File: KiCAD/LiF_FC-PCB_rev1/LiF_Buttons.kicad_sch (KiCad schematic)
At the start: 43 parts, among them J34 BTN 3V3_{EN}, J35 BTN 3V3_{EN}, SW10 TL3301PF160QG, SW11 TL3301PF160QG, SW4 TL3301PF160QG, SW5 TL3301PF160QG, SW6 TL3301PF160QG, SW7 TL3301PF160QG, SW8 TL3301PF160QG, SW9 TL3301PF160QG, U16 SN74HC14DR, U17 SN74HC14DR, U18 74HCT595PW,118

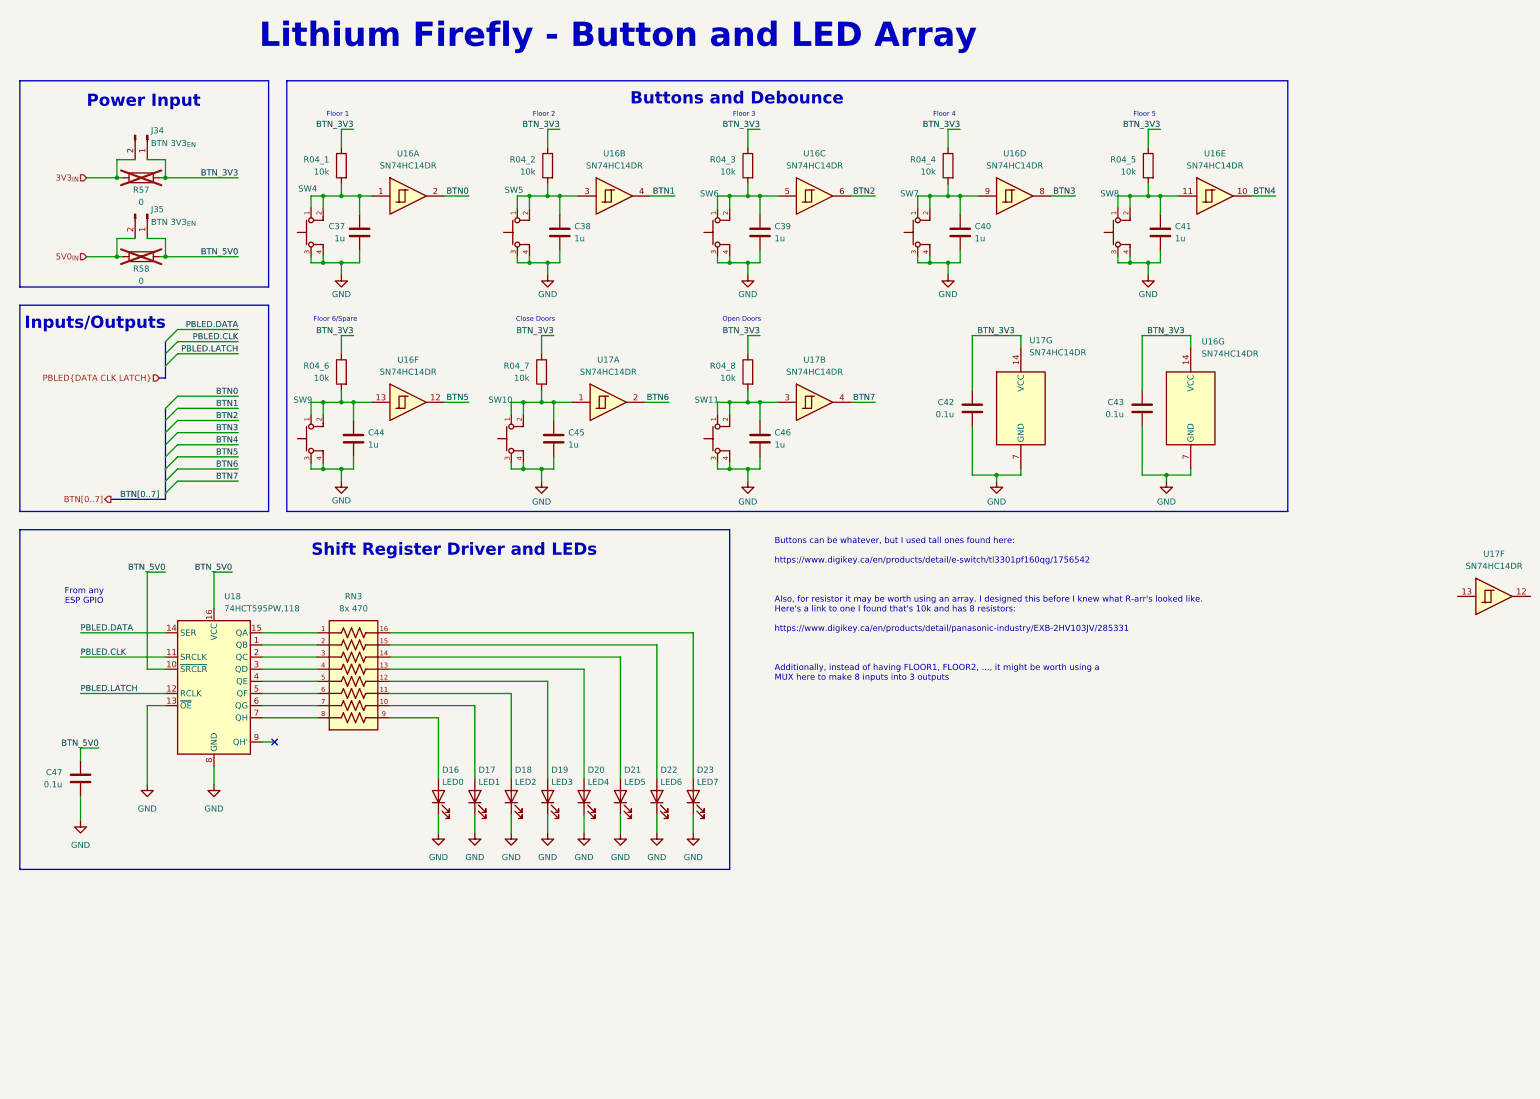
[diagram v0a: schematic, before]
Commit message: fixing ERC bugs on schematic. Only MCU left
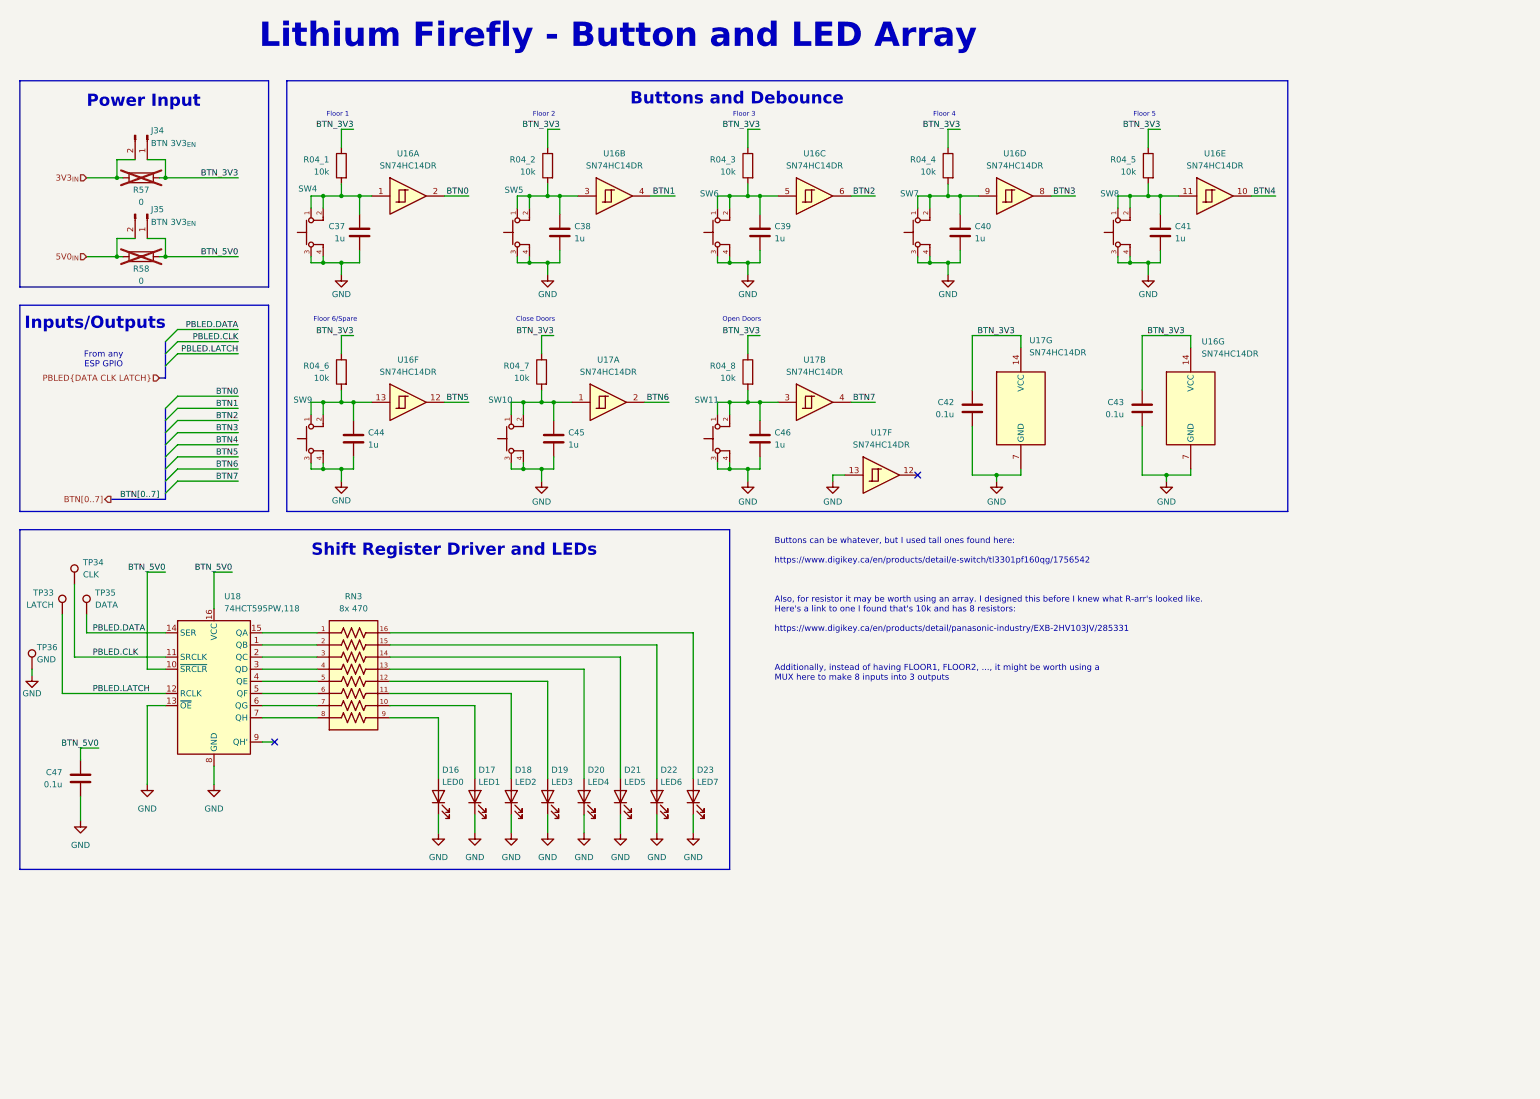
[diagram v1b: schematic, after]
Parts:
- added TP33: LATCH, TestPoint:TestPoint_Bridge_Pitch2.54mm_Drill1.0mm, symbol Connector:TestPoint
- added TP34: CLK, TestPoint:TestPoint_Bridge_Pitch2.54mm_Drill1.0mm, symbol Connector:TestPoint
- added TP35: DATA, TestPoint:TestPoint_Bridge_Pitch2.54mm_Drill1.0mm, symbol Connector:TestPoint
- added TP36: GND, TestPoint:TestPoint_Bridge_Pitch2.54mm_Drill1.0mm, symbol Connector:TestPoint
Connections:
- net GND: now also U17.13, TP36.1
- net PBLED.CLK: now also TP34.1
- net PBLED.DATA: now also TP35.1
- net PBLED.LATCH: now also TP33.1
- no-connect marks 1 -> 2
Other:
- moved on the sheet: U17F

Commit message: Added MCU pinout, shanged shift registers to GPIO expanders to save pins on MCU
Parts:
- removed C47: 0.1u, Capacitor_SMD:C_0805_2012Metric, symbol Device:C
- removed J35: BTN 3V3_{EN}, Connector_PinHeader_2.54mm:PinHeader_1x02_P2.54mm_Vertical, symbol Connector:Conn_01x02_Pin
- removed R58: 0, Resistor_SMD:R_0805_2012Metric, symbol Device:R
- removed TP33: LATCH, TestPoint:TestPoint_Bridge_Pitch2.54mm_Drill1.0mm, symbol Connector:TestPoint
- removed TP34: CLK, TestPoint:TestPoint_Bridge_Pitch2.54mm_Drill1.0mm, symbol Connector:TestPoint
- removed TP35: DATA, TestPoint:TestPoint_Bridge_Pitch2.54mm_Drill1.0mm, symbol Connector:TestPoint
- removed TP36: GND, TestPoint:TestPoint_Bridge_Pitch2.54mm_Drill1.0mm, symbol Connector:TestPoint
- removed U18: 74HCT595PW,118, Package_SO:TSSOP-16_4.4x5mm_P0.65mm, symbol 74xx:74HCT595
- added C45: 0.1u, Capacitor_SMD:C_0805_2012Metric, symbol Device:C
- added JP1: BTN3, Jumper:SolderJumper-2_P1.3mm_Open_RoundedPad1.0x1.5mm, symbol Jumper:SolderJumper_2_Open
- added JP2: BTN4, Jumper:SolderJumper-2_P1.3mm_Open_RoundedPad1.0x1.5mm, symbol Jumper:SolderJumper_2_Open
- added JP3: BTN5, Jumper:SolderJumper-2_P1.3mm_Open_RoundedPad1.0x1.5mm, symbol Jumper:SolderJumper_2_Open
- added R04_9: 10k, Resistor_SMD:R_0805_2012Metric, symbol Device:R
- added U18: NCA9555, Package_SO:TSSOP-24_4.4x7.8mm_P0.65mm, symbol Interface_Expansion:PCA9555PW
- renumbered C37 to C35, C38 to C36, C39 to C37, C40 to C38, C41 to C39, C42 to C40, C43 to C41, C44 to C42, C45 to C43, C46 to C44, U16 to U15, U17 to U16
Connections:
- net BTN0: now also U18.4 (IO0_0)
- net BTN1: now also U18.5 (IO0_1)
- net BTN2: now also U18.6 (IO0_2)
- net BTN3: now also JP1.2 (B), U18.7 (IO0_3); no longer U15.8
- net BTN4: now also JP2.1 (A), U18.8 (IO0_4); no longer U15.10
- net BTN5: now also JP3.2 (B), U18.9 (IO0_5); no longer U15.12
- net BTN6: now also U18.10 (IO0_6)
- net BTN7: now also U18.11 (IO0_7)
- net BTN_3V3: now also C45.1, R04_9.1, U18.24 (VDD)
- net GND: now also C45.2, U18.12 (VSS), U18.2 (A1), U18.21 (A0), U18.3 (A2)
- net LED1: now reaches RN3.2
- net LED1: now also U18.14 (IO1_1)
- net LED0: now reaches RN3.1
- net LED0: now also U18.13 (IO1_0)
- net LED2: now reaches RN3.3
- net LED2: now also U18.15 (IO1_2)
- net LED3: now reaches RN3.4
- net LED3: now also U18.16 (IO1_3)
- net LED4: now reaches RN3.5
- net LED4: now also U18.17 (IO1_4)
- net LED5: now reaches RN3.6
- net LED5: now also U18.18 (IO1_5)
- net LED6: now reaches RN3.7
- net LED6: now also U18.19 (IO1_6)
- net LED7: now reaches RN3.8
- net LED7: now also U18.20 (IO1_7)
- new net: JP1.1 (A), U15.8
- new net: JP2.2 (B), U15.10
- new net: JP3.1 (A), U15.12
- new net I2C.SCL: U18.22 (SCL)
- new net I2C.SDA: U18.23 (SDA)
- new net ~{BTN_IRQ}: R04_9.2, U18.1 (~{INT})
- no-connect marks 2 -> 1
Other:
- note added: "Floor Selection LEDs"
- note added: "I2C GPIO Expander"
- note added: "I2C addr 0100 000x"
- note removed: "From any ESP GPIO"
- note removed: "Shift Register Driver and LEDs"
- title: (none) -> Lithium Firefly Custom FC/CC PCB
- moved on the sheet: D16, D17, D18, D19, D20, D21, D22, D23, J34, R57, RN3

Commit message: Finalized schematic diagram. Only needs formatting fixes and resistor component sourcing info
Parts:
- renumbered C35 to C43, C36 to C44, C37 to C45, C38 to C46, C39 to C47, C40 to C48, C41 to C49, C42 to C50, C43 to C51, C44 to C52, C45 to C53, J34 to J38, R04_1 to R61, R04_2 to R62, R04_3 to R63, R04_4 to R64, R04_5 to R65, R57 to R66, R04_6 to R67, R04_7 to R68, R04_8 to R69, R04_9 to R70, U16 to U15, U15 to U16, U18 to U17

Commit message: added door limit switch and fixed I2C pull up resistors
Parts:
- added C57: 1u, Capacitor_SMD:C_0805_2012Metric, symbol Device:C
- added J43: Door Closed, symbol Connector_Generic:Conn_01x02
- added R76: 10k, Resistor_SMD:R_0805_2012Metric, symbol Device:R
- added R77: 100, Resistor_SMD:R_0805_2012Metric, symbol Device:R
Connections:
- net BTN_3V3: now also R76.1
- net GND: now also C57.2, J43.1 (Pin_1); no longer U16.13
- net DoorLS: now reaches U16.12
- new net: J43.2 (Pin_2), R76.2, R77.1
- new net: C57.1, R77.2, U16.13
- no-connect marks 1 -> 0
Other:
- note added: "Door Closed Switch"

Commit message: set up board configuration and started routing PCB
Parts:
- J43: footprint (none) -> Connector_JST:JST_PH_B2B-PH-K_1x02_P2.00mm_Vertical
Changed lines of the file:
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@@
 			)
 		)
-		(property "Footprint" ""
+		(property "Footprint" "Connector_JST:JST_PH_B2B-PH-K_1x02_P2.00mm_Vertical"
 			(at 198.12 148.59 0)
 			(effects

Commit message: backup before expanding the board size
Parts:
- removed JP1: BTN3, Jumper:SolderJumper-2_P1.3mm_Open_RoundedPad1.0x1.5mm, symbol Jumper:SolderJumper_2_Open
- removed JP2: BTN4, Jumper:SolderJumper-2_P1.3mm_Open_RoundedPad1.0x1.5mm, symbol Jumper:SolderJumper_2_Open
- removed JP3: BTN5, Jumper:SolderJumper-2_P1.3mm_Open_RoundedPad1.0x1.5mm, symbol Jumper:SolderJumper_2_Open
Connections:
- net BTN3: now also U15.8
- net BTN4: now also U15.10
- net BTN5: now also U15.12

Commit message: backup before leaving school
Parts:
- J38: footprint Connector_PinHeader_2.54mm:PinHeader_1x02_P2.54mm_Vertical -> Connector_PinHeader_2.54mm:PinHeader_1x02_P2.54mm_Vertical_SMD_Pin1Left
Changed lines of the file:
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@@
 			)
 		)
-		(property "Footprint" "Connector_PinHeader_2.54mm:PinHeader_1x02_P2.54mm_Vertical"
+		(property "Footprint" "Connector_PinHeader_2.54mm:PinHeader_1x02_P2.54mm_Vertical_SMD_Pin1Left"
 			(at 41.91 46.99 0)
 			(effects

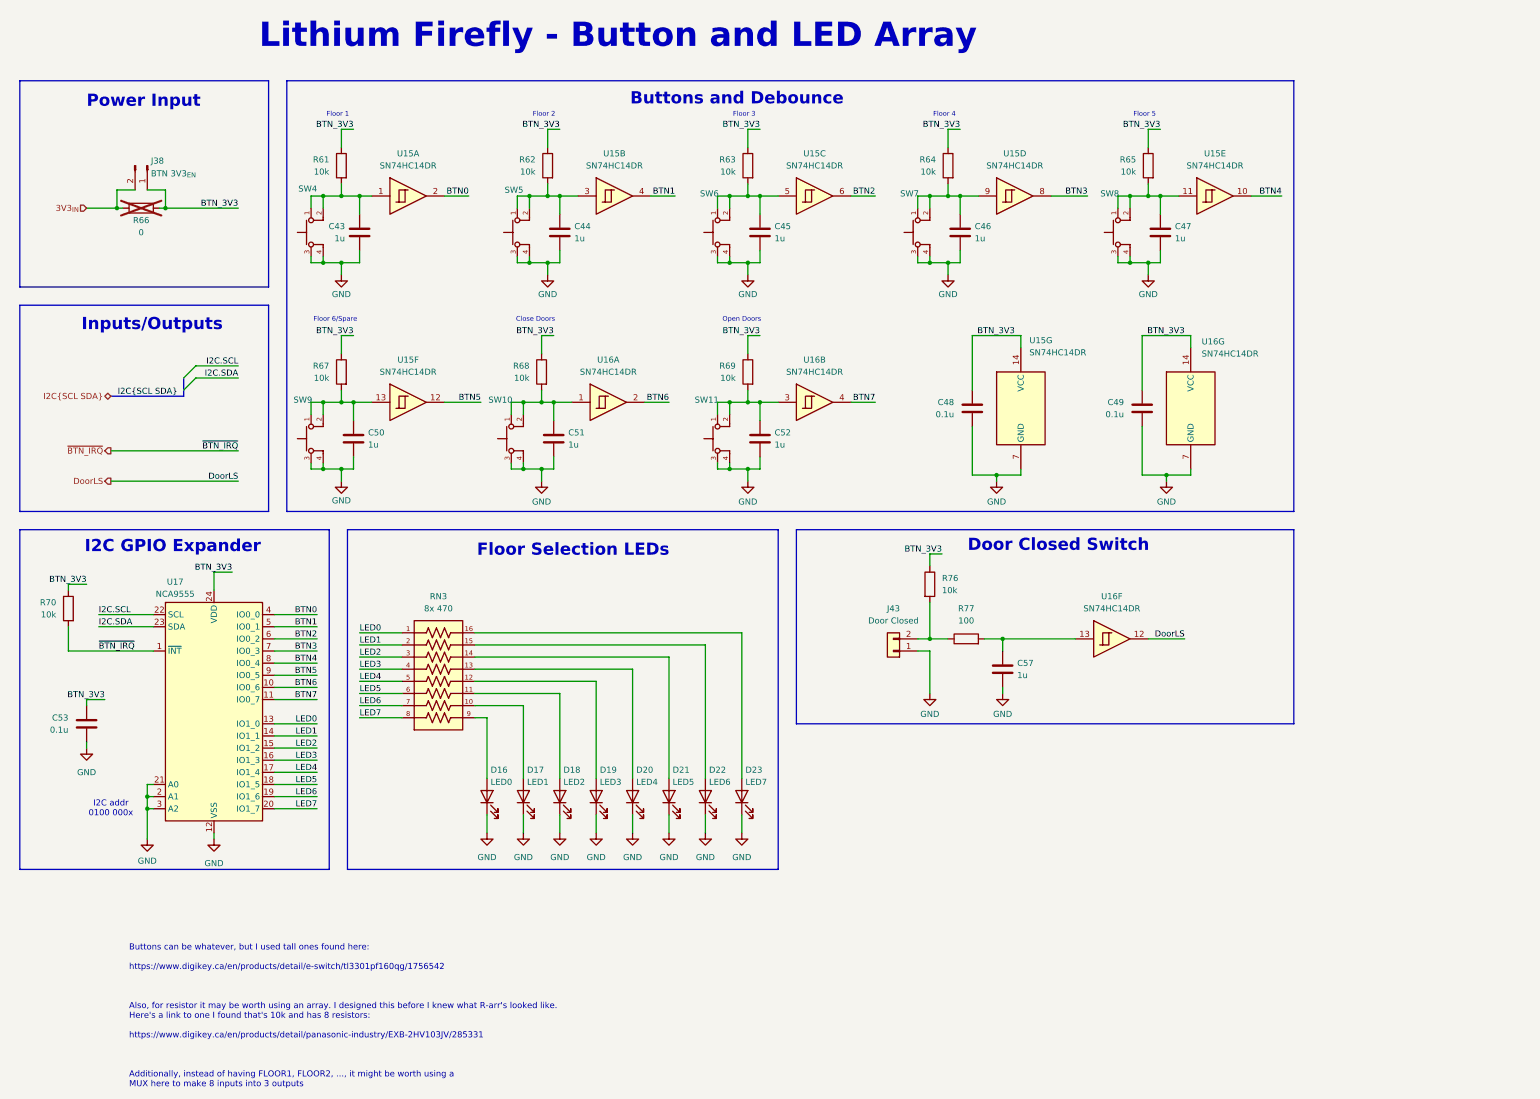
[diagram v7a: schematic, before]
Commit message: Created new KiCAD project for IO PCB, moved relevant components there, saving backup before reannotating the Service PCB schematics
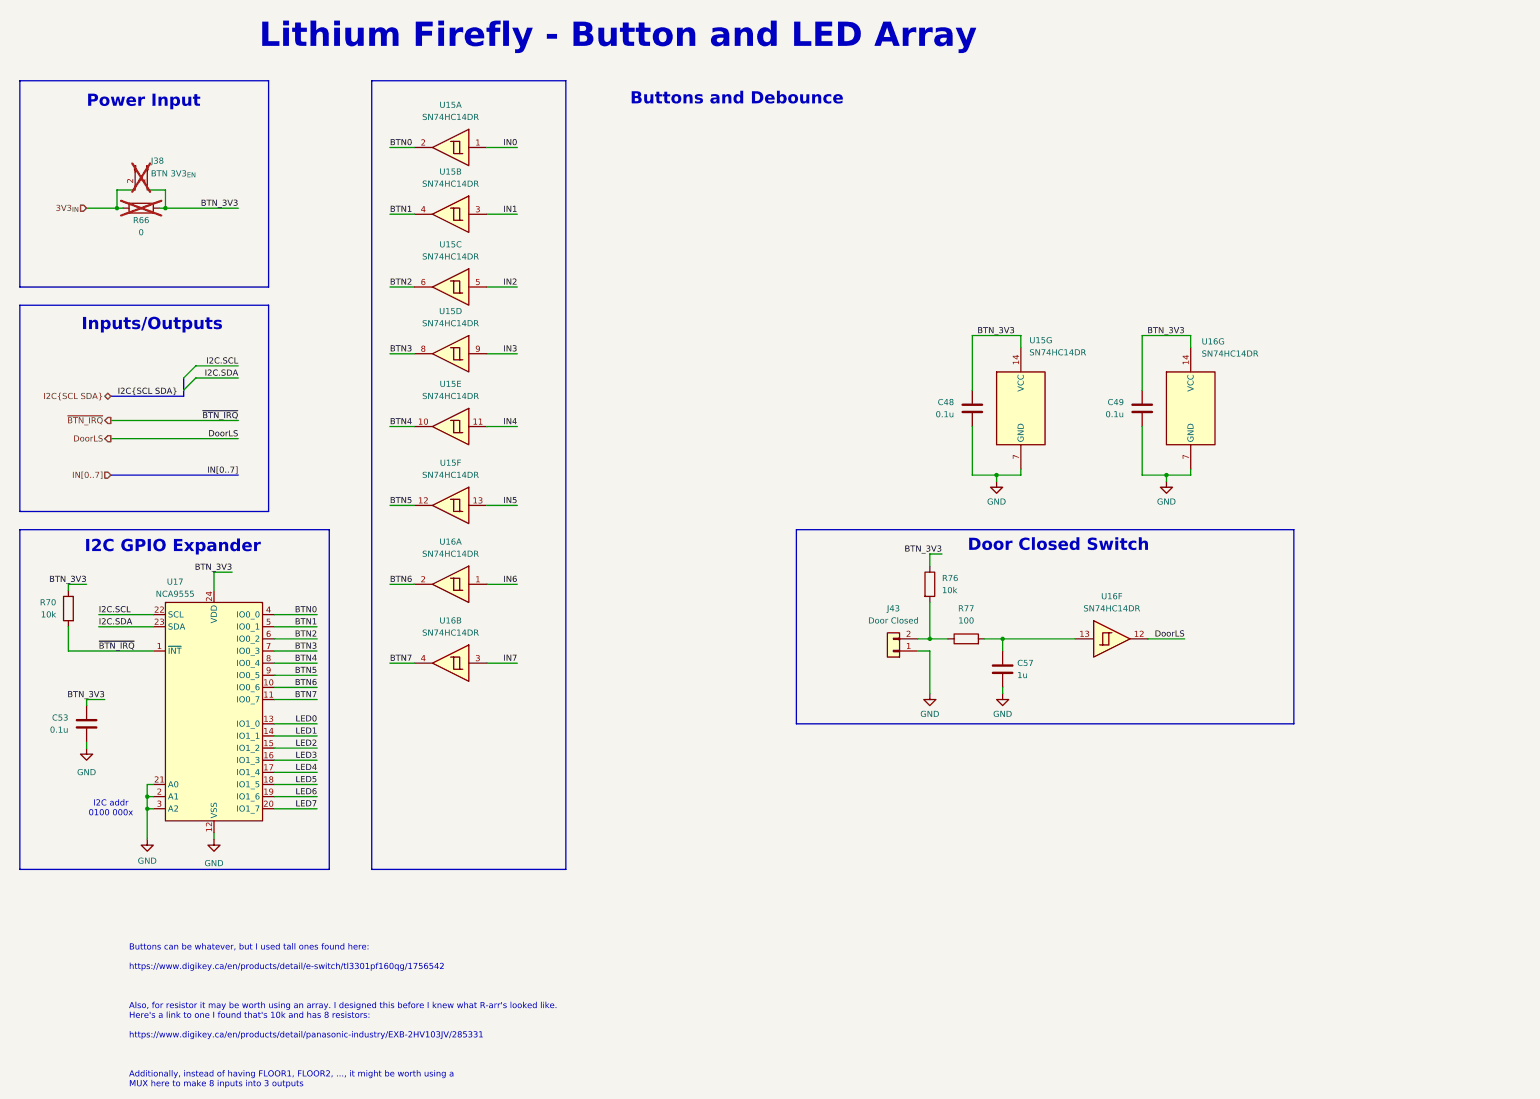
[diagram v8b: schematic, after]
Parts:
- removed C43, C44, C45, C46, C47, C50, C51, C52: 1u, Capacitor_SMD:C_0805_2012Metric, symbol Device:C
- removed D16: LED0, LED_SMD:LED_0805_2012Metric, symbol Device:LED
- removed D17: LED1, LED_SMD:LED_0805_2012Metric, symbol Device:LED
- removed D18: LED2, LED_SMD:LED_0805_2012Metric, symbol Device:LED
- removed D19: LED3, LED_SMD:LED_0805_2012Metric, symbol Device:LED
- removed D20: LED4, LED_SMD:LED_0805_2012Metric, symbol Device:LED
- removed D21: LED5, LED_SMD:LED_0805_2012Metric, symbol Device:LED
- removed D22: LED6, LED_SMD:LED_0805_2012Metric, symbol Device:LED
- removed D23: LED7, LED_SMD:LED_0805_2012Metric, symbol Device:LED
- removed R61, R62, R63, R64, R65, R67, R68, R69: 10k, Resistor_SMD:R_0805_2012Metric, symbol Device:R
- removed RN3: 8x 470, LiF_PCB_Footprints:RESCAXE50P380X160X55-16N, symbol LiF_PCB_Symbols:EXB-2HV471JV
- removed SW10, SW11, SW4, SW5, SW6, SW7, SW8, SW9: TL3301PF160QG, LiF_PCB_Footprints:SW_TL3301PF160QG, symbol LiF_PCB_Symbols:TL3301PF160QG
- J38: now not fitted; now left out of the parts list
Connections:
- net IN0: now reaches U15.1
- net IN5: now reaches U15.13
- net IN7: now reaches U16.3
- net IN4: now reaches U15.11
- net IN1: now reaches U15.3
- net IN3: now reaches U15.9
- net IN2: now reaches U15.5
- net IN6: now reaches U16.1
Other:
- note removed: "Close Doors"
- note removed: "Floor 1"
- note removed: "Floor 2"
- note removed: "Floor 3"
- note removed: "Floor 4"
- note removed: "Floor 5"
- note removed: "Floor 6/Spare"
- note removed: "Floor Selection LEDs"
- note removed: "Open Doors"
- moved on the sheet: U15A, U15B, U15C, U15D, U15E, U15F, U16A, U16B
